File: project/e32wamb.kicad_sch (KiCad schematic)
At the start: 31 parts, among them J1 2059-302_998-403, J2 Conn_01x04, J3 Conn_01x03, Q1 AO3400, Q2 AO3400, Q3 AO3400, Q4 AO3400, Q5 AO3400, SW1 TS-1187A-B-A-B, U1 AP63203WU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

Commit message: Switch the esp32-c6 to DIP footprint
Sam suggested it might make the debugging a bit easier.
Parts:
- U2: value XIAO-ESP32-C6-SMD -> XIAO-ESP32-C6-DIP; footprint xiao:XIAO-ESP32C6-SMD -> xiao:XIAO-ESP32C6-DIP; symbol xiao:XIAO-ESP32-C6-SMD -> xiao:XIAO_ESP32-C6-DIP; SKU (none) -> XIAO-DIP; now in the parts list
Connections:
- no-connect marks 16 -> 6

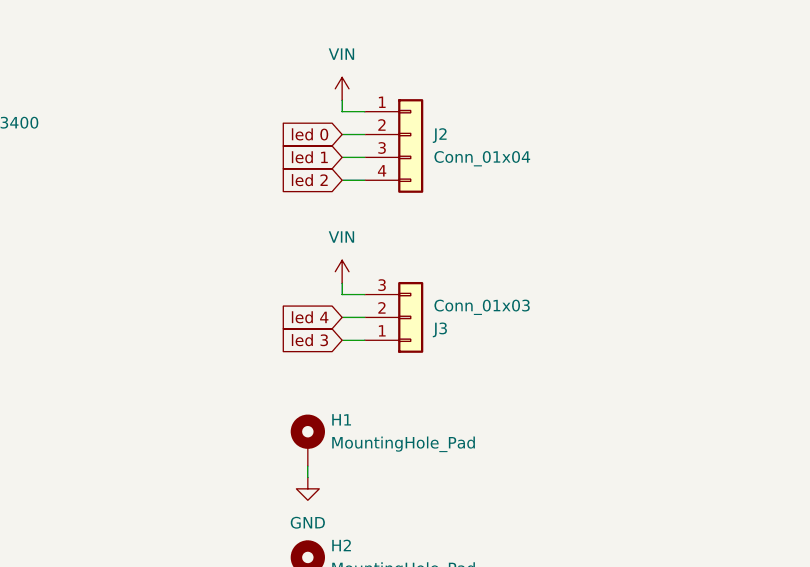
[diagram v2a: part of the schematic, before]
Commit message: Switch J3 to 4-pin JST PH
Not only will that give me two additional independent chans, but
also one less BOM part to deal with (cheaper for PCBA).
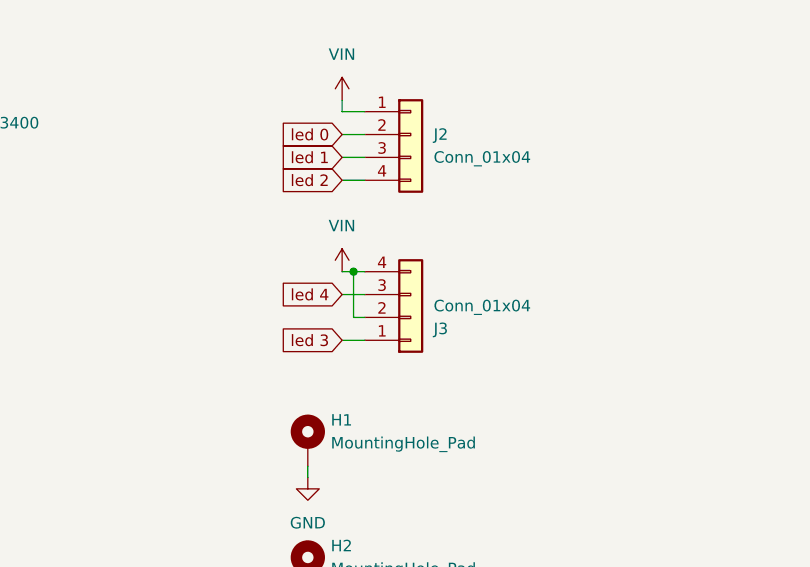
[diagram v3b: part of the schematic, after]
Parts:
- J3: value Conn_01x03 -> Conn_01x04; footprint misc-lib:JST_PH_S3B-PH-SM4-TB_1x03-1MP_P2.00mm_Horizontal -> misc-lib:JST_PH_S4B-PH-SM4-TB_1x04-1MP_P2.00mm_Horizontal; symbol Connector_Generic:Conn_01x03 -> Connector_Generic:Conn_01x04
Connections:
- net VIN: now also J3.2 (Pin_2), J3.4 (Pin_4); no longer J3.3 (Pin_3)
- net led 4: now also J3.3 (Pin_3); no longer J3.2 (Pin_2)
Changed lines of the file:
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@@
 	)
 	(junction
+		(at 127 146.05)
+		(diameter 0)
+		(color 0 0 0 0)
+	)
+	(junction
 		(at 261.62 101.6)
 		(diameter 0)
@@
 	(wire
 		(pts
+			(xy 127 151.13) (xy 127 146.05)
+		)
+		(stroke
+			(width 0)
+			(type default)
+		)
+	)
+	(wire
+		(pts
 			(xy 77.47 40.64) (xy 81.28 40.64)
 		)
@@
 	(wire
 		(pts
-			(xy 35.56 40.64) (xy 35.56 53.34)
+			(xy 125.73 146.05) (xy 127 146.05)
 		)
 		(stroke
@@
 	(wire
 		(pts
-			(xy 207.01 52.07) (xy 208.28 52.07)
+			(xy 35.56 40.64) (xy 35.56 53.34)
 		)
 		(stroke
@@
 	(wire
 		(pts
-			(xy 26.67 49.53) (xy 26.67 58.42)
+			(xy 207.01 52.07) (xy 208.28 52.07)
 		)
 		(stroke
@@
 	(wire
 		(pts
-			(xy 29.21 138.43) (xy 33.02 138.43)
+			(xy 26.67 49.53) (xy 26.67 58.42)
 		)
 		(stroke
@@
 	(wire
 		(pts
-			(xy 125.73 151.13) (xy 128.27 151.13)
+			(xy 29.21 138.43) (xy 33.02 138.43)
 		)
 		(stroke
@@
 	(wire
 		(pts
-			(xy 125.73 147.32) (xy 125.73 148.59)
-		)
-		(stroke
-			(width 0)
-			(type default)
-		)
-	)
-	(wire
-		(pts
 			(xy 92.71 31.75) (xy 92.71 40.64)
 		)
@@
 	(wire
 		(pts
+			(xy 128.27 151.13) (xy 127 151.13)
+		)
+		(stroke
+			(width 0)
+			(type default)
+		)
+	)
+	(wire
+		(pts
 			(xy 72.39 101.6) (xy 72.39 100.33)
 		)
@@
 	(wire
 		(pts
+			(xy 127 146.05) (xy 128.27 146.05)
+		)
+		(stroke
+			(width 0)
+			(type default)
+		)
+	)
+	(wire
+		(pts
 			(xy 33.02 97.79) (xy 33.02 99.06)
 		)
@@
 	(global_label "led 4"
 		(shape input)
-		(at 125.73 151.13 180)
+		(at 125.73 148.59 180)
 		(fields_autoplaced yes)
 		(effects
@@
 		)
 		(property "Intersheetrefs" "${INTERSHEET_REFS}"
-			(at 117.6649 151.13 0)
+			(at 117.6649 148.59 0)
 			(effects
 				(font
@@
 	(symbol
 		(lib_id "power:VDC")
-		(at 125.73 147.32 0)
+		(at 125.73 146.05 0)
 		(unit 1)
 		(exclude_from_sim no)
@@
 		(fields_autoplaced yes)
 		(property "Reference" "#PWR023"
-			(at 125.73 151.13 0)
+			(at 125.73 149.86 0)
 			(effects
 				(font
@@
 		)
 		(property "Value" "VIN"
-			(at 125.73 142.24 0)
+			(at 125.73 140.97 0)
 			(effects
 				(font
@@
 		)
 		(property "Footprint" ""
-			(at 125.73 147.32 0)
+			(at 125.73 146.05 0)
 			(effects
 				(font
@@
 		)
 		(property "Datasheet" ""
-			(at 125.73 147.32 0)
+			(at 125.73 146.05 0)
 			(effects
 				(font
@@
 		)
 		(property "Description" "Power symbol creates a global label with name \"VDC\""
-			(at 125.73 147.32 0)
+			(at 125.73 146.05 0)
 			(effects
 				(font
@@
 	)
 	(symbol
-		(lib_id "Connector_Generic:Conn_01x03")
+		(lib_id "Connector_Generic:Conn_01x04")
 		(at 133.35 151.13 0)
 		(mirror x)
@@
 			)
 		)
-		(property "Value" "Conn_01x03"
+		(property "Value" "Conn_01x04"
 			(at 135.89 149.8601 0)
 			(effects
@@
 			)
 		)
-		(property "Footprint" "misc-lib:JST_PH_S3B-PH-SM4-TB_1x03-1MP_P2.00mm_Horizontal"
+		(property "Footprint" "misc-lib:JST_PH_S4B-PH-SM4-TB_1x04-1MP_P2.00mm_Horizontal"
 			(at 133.35 151.13 0)
 			(effects
@@
 			)
 		)
-		(property "Datasheet" "https://jlcpcb.com/api/file/downloadByFileSystemAccessId/8588902717552513024"
+		(property "Datasheet" "~"
 			(at 133.35 151.13 0)
 			(effects
@@
 			)
 		)
-		(property "Description" "JST PH 3p"
+		(property "Description" "Generic connector, single row, 01x04, script generated (kicad-library-utils/schlib/autogen/connector/)"
 			(at 133.35 151.13 0)
 			(effects
@@
 		(pin "3"
 		)
+		(pin "4"
+		)
 		(instances

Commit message: Fix wrong J3 LCSC part number
Forgot to fix this in 7358522f.
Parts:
- J3: LCSC C265101 -> C265102
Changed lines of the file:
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@@
 			)
 		)
-		(property "LCSC" "C265101"
+		(property "LCSC" "C265102"
 			(at 133.35 151.13 0)
 			(effects
